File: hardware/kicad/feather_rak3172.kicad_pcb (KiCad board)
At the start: 2 copper layers, 51 x 23.1 mm, 53 parts, among them J1 Pin Header, J2 Pin Header, J3 USB_C_Receptacle_USB2.0, J4 SMA-KE-P903, J5 SWD, J6 JST-2PH, Q1 DMG3415UQ-7, SW1 RESET, SW2 BOOT, U1 RAK3172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

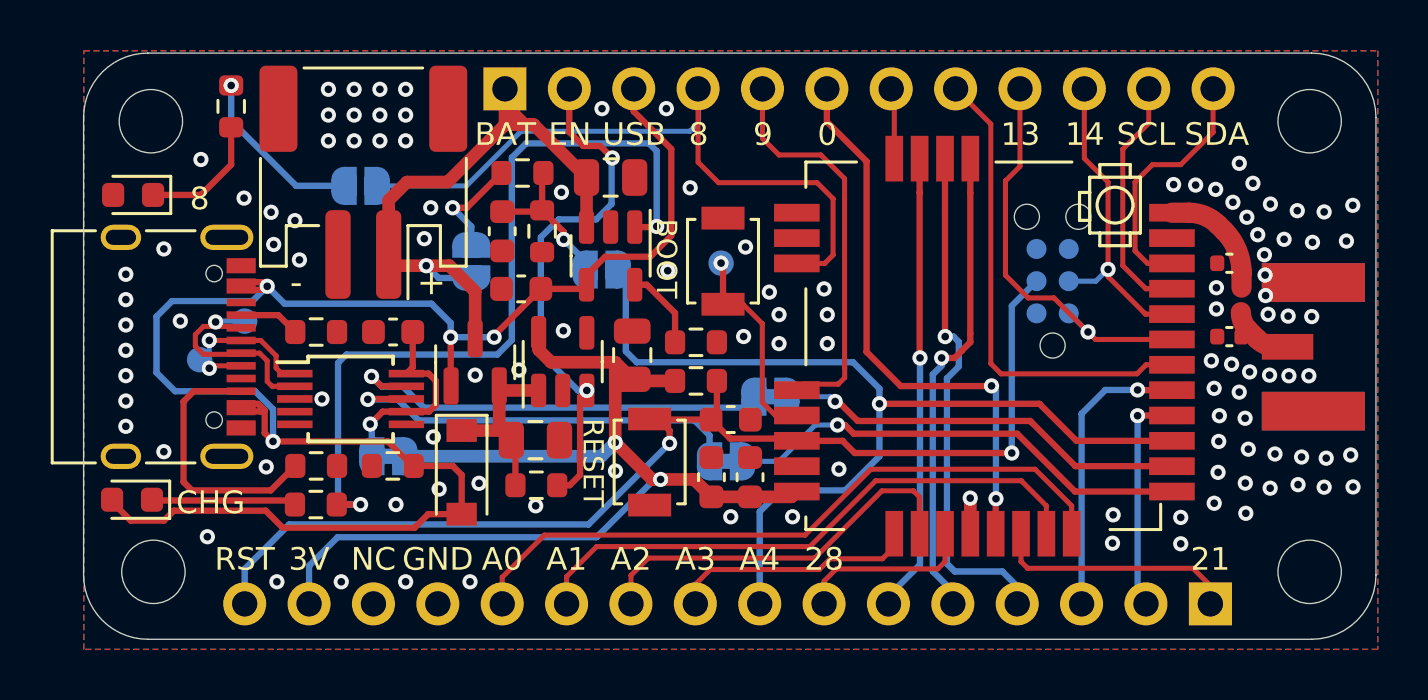
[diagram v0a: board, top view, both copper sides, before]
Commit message: fix components position
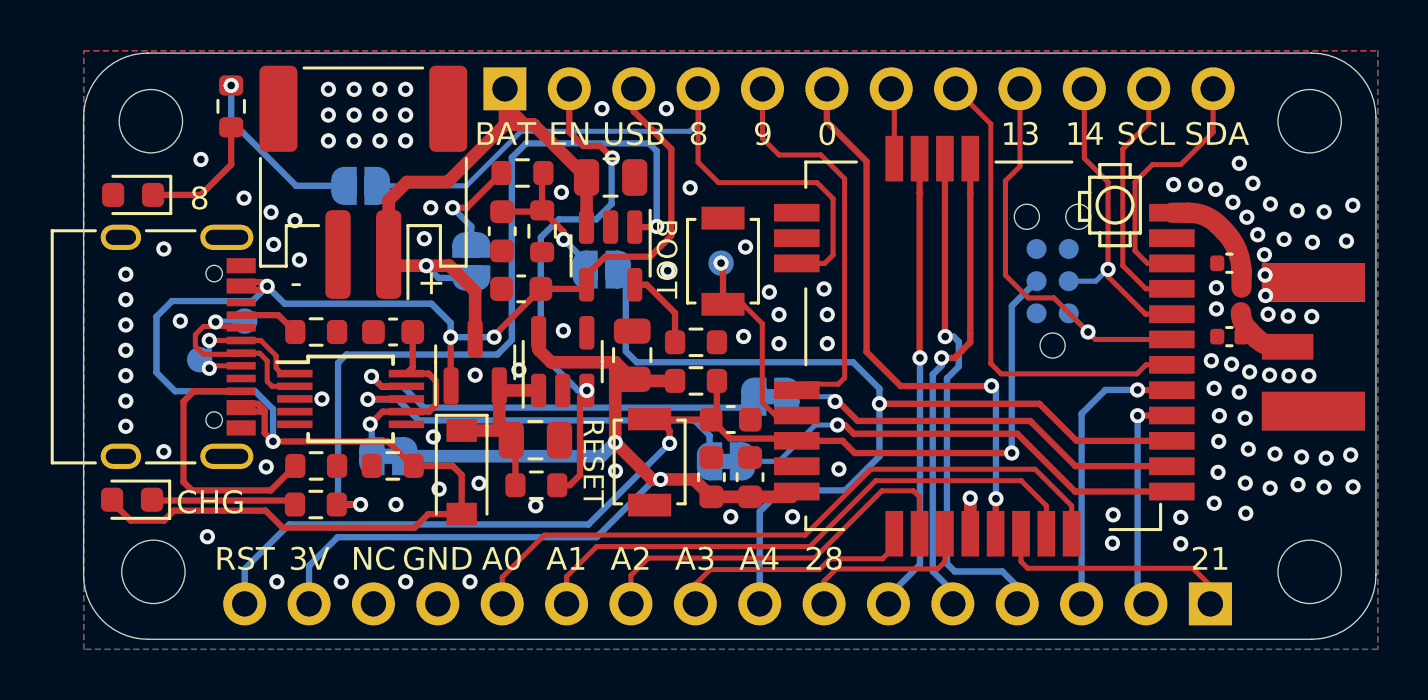
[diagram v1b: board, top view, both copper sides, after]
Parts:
- J4: footprint Teapot:SMA_HJTech_023 -> Teapot:SMA-KE-P903
- moved U1 10.8 mm to (152.4, 102.3)
- moved J4 1.59 mm to (167.4, 102.4)
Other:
- board text added: "Rev 8.4"
- board text removed: "Rev 8.3"

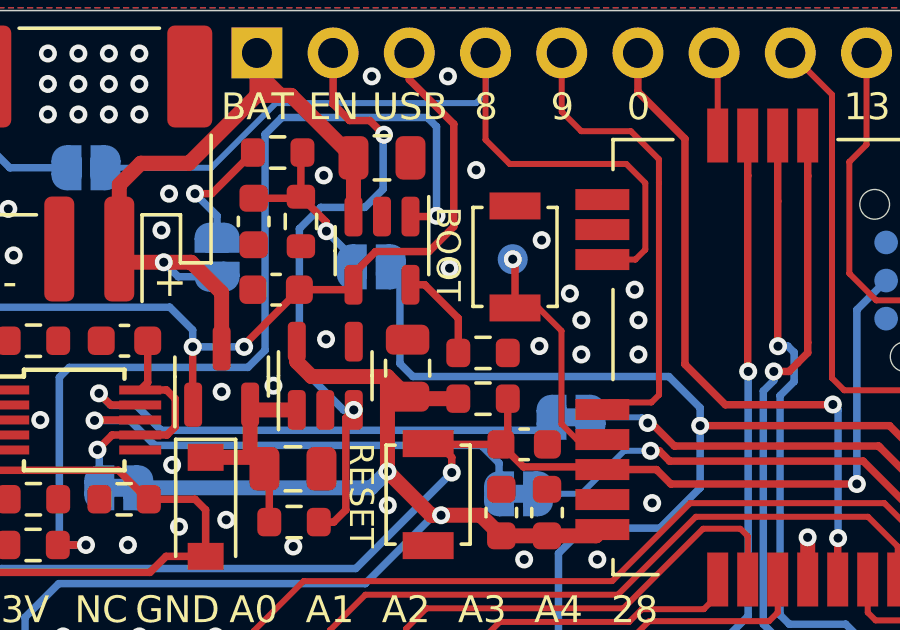
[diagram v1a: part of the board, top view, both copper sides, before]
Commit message: change boot button to 3v3
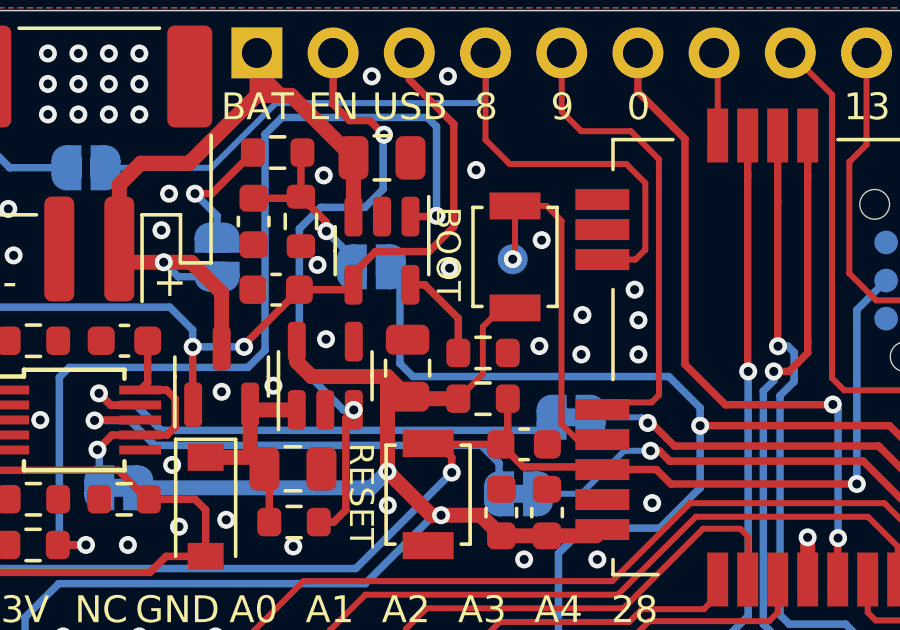
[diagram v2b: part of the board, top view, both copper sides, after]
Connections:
- SW2 pad 1: /BOOT0 -> +3.3V
- SW2 pad 2: GND -> /BOOT0
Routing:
- net +3.3V: track 43.2 -> 47.3 mm
- net /BOOT0: track 8.21 -> 11.9 mm
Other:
- board text added: "Rev 9"
- board text removed: "Rev 8.4"
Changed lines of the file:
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@@
   (title_block
     (title "Feather RAK3172")
-    (date "2023-03-20")
-    (rev "8.4")
+    (date "2023-03-21")
+    (rev "9")
     (company "Teapot Laboratories")
   )
@@
     (fp_circle (center 0 0) (end 0.75 0) (layer "F.Fab") (width 0.1) (fill none))
     (pad "1" smd rect (at -1.7 0 90) (size 0.9 1.7) (layers "F.Cu" "F.Paste" "F.Mask")
-      (net 35 "/BOOT0") (pinfunction "1") (pintype "passive"))
+      (net 2 "+3.3V") (pinfunction "1") (pintype "passive"))
     (pad "2" smd rect (at 1.7 0 90) (size 0.9 1.7) (layers "F.Cu" "F.Paste" "F.Mask")
-      (net 1 "GND") (pinfunction "2") (pintype "passive"))
+      (net 35 "/BOOT0") (pinfunction "2") (pintype "passive"))
     (model "${KICAD6_3DMODEL_DIR}/Button_Switch_SMD.3dshapes/SW_SPST_B3U-1000P.wrl"
       (offset (xyz 0 0 0))
@@
     (effects (font (size 0.89408 0.89408) (thickness 0.15)) (justify mirror))
   )
-  (gr_text "Rev 8.4" (at 128.524 104.648) (layer "B.SilkS")
+  (gr_text "Rev 9" (at 128.524 104.648) (layer "B.SilkS")
     (effects (font (size 0.8 0.8) (thickness 0.1)) (justify mirror))
   )
@@
   (via (at 118.5 100.5) (size 0.6) (drill 0.3) (layers "F.Cu" "B.Cu") (free) (net 1))
   (via (at 163.16 97.94) (size 0.6) (drill 0.3) (layers "F.Cu" "B.Cu") (free) (net 1))
-  (via (at 143.891 100.203) (size 0.6) (drill 0.3) (layers "F.Cu" "B.Cu") (free) (net 1))
   (via (at 144.272 102.235) (size 0.6) (drill 0.3) (layers "F.Cu" "B.Cu") (free) (net 1))
   (via (at 163.6268 103.4796) (size 0.6) (drill 0.3) (layers "F.Cu" "B.Cu") (free) (net 1))
@@
   (via (at 126.492 93.218) (size 0.6) (drill 0.3) (layers "F.Cu" "B.Cu") (free) (net 1))
   (via (at 120 106.5) (size 0.6) (drill 0.3) (layers "F.Cu" "B.Cu") (free) (net 1))
+  (via (at 135.48 99.25) (size 0.6) (drill 0.3) (layers "F.Cu" "B.Cu") (free) (net 1))
   (via (at 162.97 95.91) (size 0.6) (drill 0.3) (layers "F.Cu" "B.Cu") (free) (net 1))
   (via (at 127 111.633) (size 0.6) (drill 0.3) (layers "F.Cu" "B.Cu") (free) (net 1))
@@
   (via (at 118.5 99.5) (size 0.6) (drill 0.3) (layers "F.Cu" "B.Cu") (free) (net 1))
   (via (at 165.1762 103.505) (size 0.6) (drill 0.3) (layers "F.Cu" "B.Cu") (free) (net 1))
-  (via (at 144.272 101.092) (size 0.6) (drill 0.3) (layers "F.Cu" "B.Cu") (free) (net 1))
+  (via (at 144.31 100.92) (size 0.6) (drill 0.3) (layers "F.Cu" "B.Cu") (free) (net 1))
   (via (at 162.8394 103.3526) (size 0.6) (drill 0.3) (layers "F.Cu" "B.Cu") (free) (net 1))
   (via (at 166.8272 106.6292) (size 0.6) (drill 0.3) (layers "F.Cu" "B.Cu") (free) (net 1))
@@
   (via (at 144.8054 109.0676) (size 0.6) (drill 0.3) (layers "F.Cu" "B.Cu") (free) (net 1))
   (segment (start 143.129 108.2808) (end 144.7654 108.2808) (width 0.5) (layer "F.Cu") (net 2))
+  (segment (start 141.6162 100.6838) (end 140.99 101.31) (width 0.2) (layer "F.Cu") (net 2))
   (segment (start 137.8102 102.9716) (end 137.8102 106.1364) (width 0.5) (layer "F.Cu") (net 2))
+  (segment (start 140.99 101.31) (end 140.99 102.8886) (width 0.2) (layer "F.Cu") (net 2))
   (segment (start 134.7876 102.4788) (end 135.2804 102.9716) (width 0.5) (layer "F.Cu") (net 2))
   (segment (start 139.5984 107.5944) (end 140.9186 107.5944) (width 0.5) (layer "F.Cu") (net 2))
   (segment (start 138.5468 103.7082) (end 138.4808 103.6422) (width 0.5) (layer "F.Cu") (net 2))
   (segment (start 135.2804 102.9716) (end 137.8102 102.9716) (width 0.5) (layer "F.Cu") (net 2))
+  (segment (start 142.0622 100.6838) (end 141.6162 100.6838) (width 0.2) (layer "F.Cu") (net 2))
   (segment (start 137.8102 106.1364) (end 139.2682 107.5944) (width 0.5) (layer "F.Cu") (net 2))
   (segment (start 141.605 108.2808) (end 143.129 108.2808) (width 0.5) (layer "F.Cu") (net 2))
   (segment (start 139.2682 107.5944) (end 139.5984 107.5944) (width 0.5) (layer "F.Cu") (net 2))
+  (segment (start 140.99 102.8886) (end 140.1704 103.7082) (width 0.2) (layer "F.Cu") (net 2))
   (segment (start 137.8102 102.9716) (end 138.4808 103.6422) (width 0.5) (layer "F.Cu") (net 2))
   (segment (start 140.9186 107.5944) (end 141.605 108.2808) (width 0.5) (layer "F.Cu") (net 2))
@@
   (segment (start 126.873 108.331) (end 126.873 102.997) (width 0.25) (layer "B.Cu") (net 34))
   (segment (start 139.1412 94.3356) (end 139.446 94.6404) (width 0.25) (layer "B.Cu") (net 34))
-  (segment (start 142.0622 100.6838) (end 142.0622 99.1362) (width 0.25) (layer "F.Cu") (net 35))
-  (segment (start 142.0622 99.1362) (end 141.986 99.06) (width 0.25) (layer "F.Cu") (net 35))
-  (segment (start 142.8478 100.6838) (end 142.0622 100.6838) (width 0.2) (layer "F.Cu") (net 35))
-  (segment (start 143.6116 104.555728) (end 143.6116 101.4476) (width 0.2) (layer "F.Cu") (net 35))
-  (segment (start 143.6116 101.4476) (end 142.8478 100.6838) (width 0.2) (layer "F.Cu") (net 35))
-  (segment (start 144.127472 105.0716) (end 143.6116 104.555728) (width 0.2) (layer "F.Cu") (net 35))
+  (segment (start 142.0622 97.2838) (end 142.0622 98.9838) (width 0.2) (layer "F.Cu") (net 35))
+  (segment (start 143.6116 104.555728) (end 143.6116 97.7832) (width 0.2) (layer "F.Cu") (net 35))
+  (segment (start 142.0622 98.9838) (end 141.986 99.06) (width 0.2) (layer "F.Cu") (net 35))
+  (segment (start 143.6116 97.7832) (end 143.1122 97.2838) (width 0.2) (layer "F.Cu") (net 35))
   (segment (start 144.9746 105.0716) (end 144.127472 105.0716) (width 0.2) (layer "F.Cu") (net 35))
+  (segment (start 143.1122 97.2838) (end 142.0622 97.2838) (width 0.2) (layer "F.Cu") (net 35))
+  (segment (start 144.127472 105.0716) (end 143.6116 104.555728) (width 0.2) (layer "F.Cu") (net 35))
   (via (at 141.986 99.06) (size 0.6) (drill 0.3) (layers "F.Cu" "B.Cu") (net 35))
   (segment (start 159.7746 108.0716) (end 155.9506 108.0716) (width 0.25) (layer "F.Cu") (net 36))

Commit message: minor schematic changes
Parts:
- J1, J2: value Pin Header -> DNP
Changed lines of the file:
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@@
       (effects (font (size 1 1) (thickness 0.15)) (justify mirror))
     )
-    (fp_text value "Pin Header" (at -2.775949 -2.431051 180) (layer "B.Fab")
+    (fp_text value "DNP" (at -2.775949 -2.431051 180) (layer "B.Fab")
       (effects (font (size 1 1) (thickness 0.15)) (justify mirror))
     )
@@
       (effects (font (size 1 1) (thickness 0.15)) (justify mirror))
     )
-    (fp_text value "Pin Header" (at -2.812051 -5.588 180) (layer "B.Fab")
+    (fp_text value "DNP" (at -2.812051 -5.588 180) (layer "B.Fab")
       (effects (font (size 1 1) (thickness 0.15)) (justify mirror))
     )

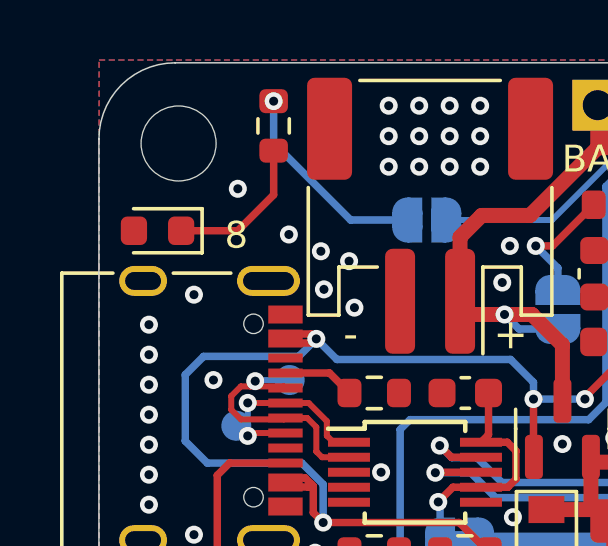
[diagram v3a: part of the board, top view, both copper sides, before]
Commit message: fix D1 polarity
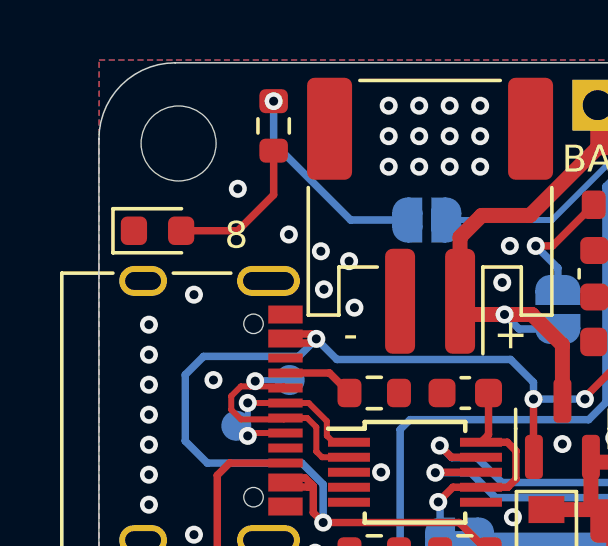
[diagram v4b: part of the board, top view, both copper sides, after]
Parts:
- turned D1 to 0 degrees
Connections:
- D1 pad 1: Net-(D1-Pad1) -> GND
- D1 pad 2: GND -> Net-(R2-Pad2)
- R2 pad 2: Net-(D1-Pad1) -> Net-(R2-Pad2)
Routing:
- net Net-(R2-Pad2): track 0.00 -> 5.05 mm
- net Net-(D1-Pad1): track 5.05 -> 0.00 mm
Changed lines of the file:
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@@
   (net 16 "Net-(C9-Pad2)")
   (net 17 "Net-(C11-Pad1)")
-  (net 18 "Net-(D1-Pad1)")
+  (net 18 "Net-(R2-Pad2)")
   (net 19 "Net-(D2-Pad1)")
   (net 20 "/TXD")
@@
       (net 52 "Net-(JP2-Pad1)") (pintype "passive"))
     (pad "2" smd roundrect (at 0.825 0 270) (size 0.8 0.95) (layers "F.Cu" "F.Paste" "F.Mask") (roundrect_rratio 0.25)
-      (net 18 "Net-(D1-Pad1)") (pintype "passive"))
+      (net 18 "Net-(R2-Pad2)") (pintype "passive"))
     (model "${KICAD6_3DMODEL_DIR}/Resistor_SMD.3dshapes/R_0603_1608Metric.wrl"
       (offset (xyz 0 0 0))
@@
   )
   (footprint "LED_SMD:LED_0603_1608Metric" (layer "F.Cu")
-    (at 118.7865 96.3695 180)
+    (at 118.7865 96.3695)
     (descr "LED SMD 0603 (1608 Metric), square (rectangular) end terminal, IPC_7351 nominal, (Body size source: http://www.tortai-tech.com/upload/download/2011102023233369053.pdf), generated with kicad-footprint-generator")
     (tags "LED")
@@
     (fp_line (start -0.8 0.4) (end 0.8 0.4) (layer "F.Fab") (width 0.1))
     (fp_line (start 0.8 -0.4) (end -0.5 -0.4) (layer "F.Fab") (width 0.1))
-    (pad "1" smd roundrect (at -0.7875 0 180) (size 0.875 0.95) (layers "F.Cu" "F.Paste" "F.Mask") (roundrect_rratio 0.25)
-      (net 18 "Net-(D1-Pad1)") (pinfunction "K") (pintype "passive"))
-    (pad "2" smd roundrect (at 0.7875 0 180) (size 0.875 0.95) (layers "F.Cu" "F.Paste" "F.Mask") (roundrect_rratio 0.25)
-      (net 1 "GND") (pinfunction "A") (pintype "passive"))
+    (pad "1" smd roundrect (at -0.7875 0) (size 0.875 0.95) (layers "F.Cu" "F.Paste" "F.Mask") (roundrect_rratio 0.25)
+      (net 1 "GND") (pinfunction "K") (pintype "passive"))
+    (pad "2" smd roundrect (at 0.7875 0) (size 0.875 0.95) (layers "F.Cu" "F.Paste" "F.Mask") (roundrect_rratio 0.25)
+      (net 18 "Net-(R2-Pad2)") (pinfunction "A") (pintype "passive"))
     (model "${KICAD6_3DMODEL_DIR}/LED_SMD.3dshapes/LED_0603_1608Metric.wrl"
       (offset (xyz 0 0 0))

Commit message: update revision version to 9.1
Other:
- board text added: "Rev 9.1"
- board text removed: "Rev 9"
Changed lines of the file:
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@@
   (title_block
     (title "Feather RAK3172")
-    (date "2023-03-21")
-    (rev "9")
+    (date "2023-05-21")
+    (rev "9.1")
     (company "Teapot Laboratories")
   )
@@
     (effects (font (size 0.89408 0.89408) (thickness 0.15)) (justify mirror))
   )
-  (gr_text "Rev 9" (at 128.524 104.648) (layer "B.SilkS")
+  (gr_text "Rev 9.1" (at 128 104.648) (layer "B.SilkS")
     (effects (font (size 0.8 0.8) (thickness 0.1)) (justify mirror))
   )
@@
   (via (at 137.8204 107.2642) (size 0.6) (drill 0.3) (layers "F.Cu" "B.Cu") (free) (net 1))
   (via (at 162.67 107.74) (size 0.6) (drill 0.3) (layers "F.Cu" "B.Cu") (free) (net 1))
-  (via (at 126.238 104.4194) (size 0.6) (drill 0.3) (layers "F.Cu" "B.Cu") (free) (net 1))
+  (via (at 126.27 103.03) (size 0.6) (drill 0.3) (layers "F.Cu" "B.Cu") (free) (net 1))
   (via (at 164.3888 103.505) (size 0.6) (drill 0.3) (layers "F.Cu" "B.Cu") (free) (net 1))
   (via (at 164.2 98.12) (size 0.6) (drill 0.3) (layers "F.Cu" "B.Cu") (free) (net 1))
